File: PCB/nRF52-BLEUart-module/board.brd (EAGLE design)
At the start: 39 x 18 mm, 44 parts, among them J1 USB-A_PTH_MALE, U1 CH340E, U2 NRF52832, Y1 32MHz_2016, Y2 32.768kHz

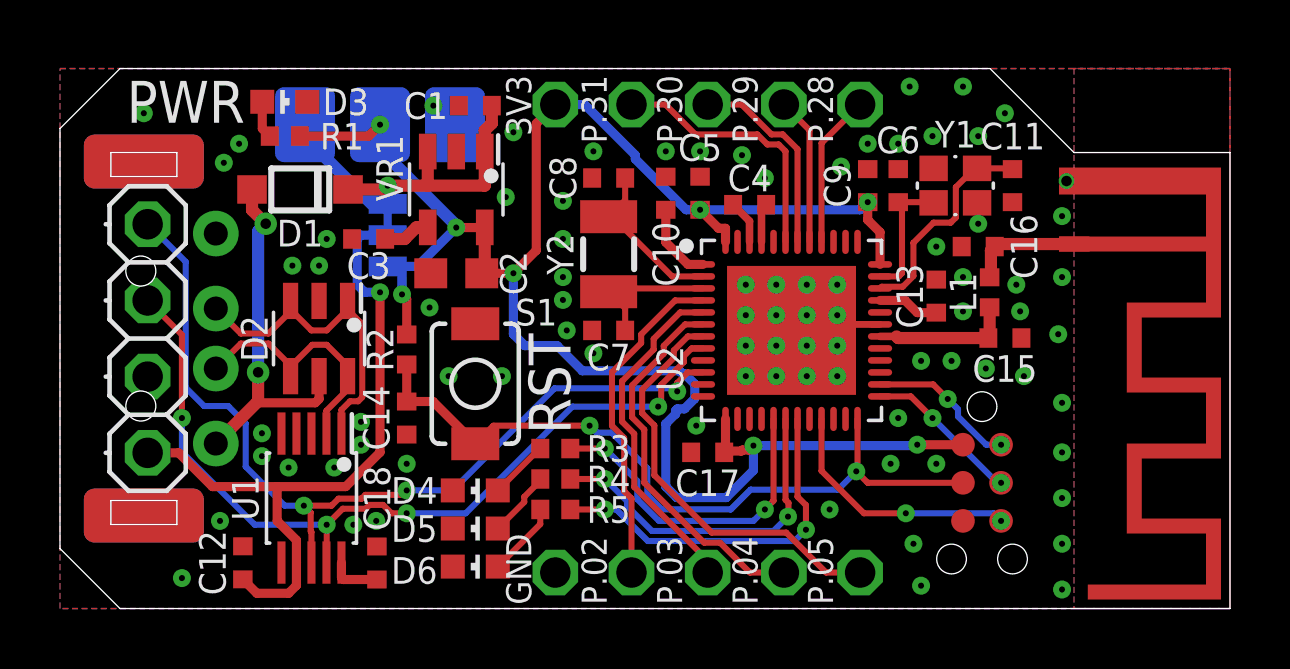
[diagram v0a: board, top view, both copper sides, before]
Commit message: PCB bug fixes, added production files
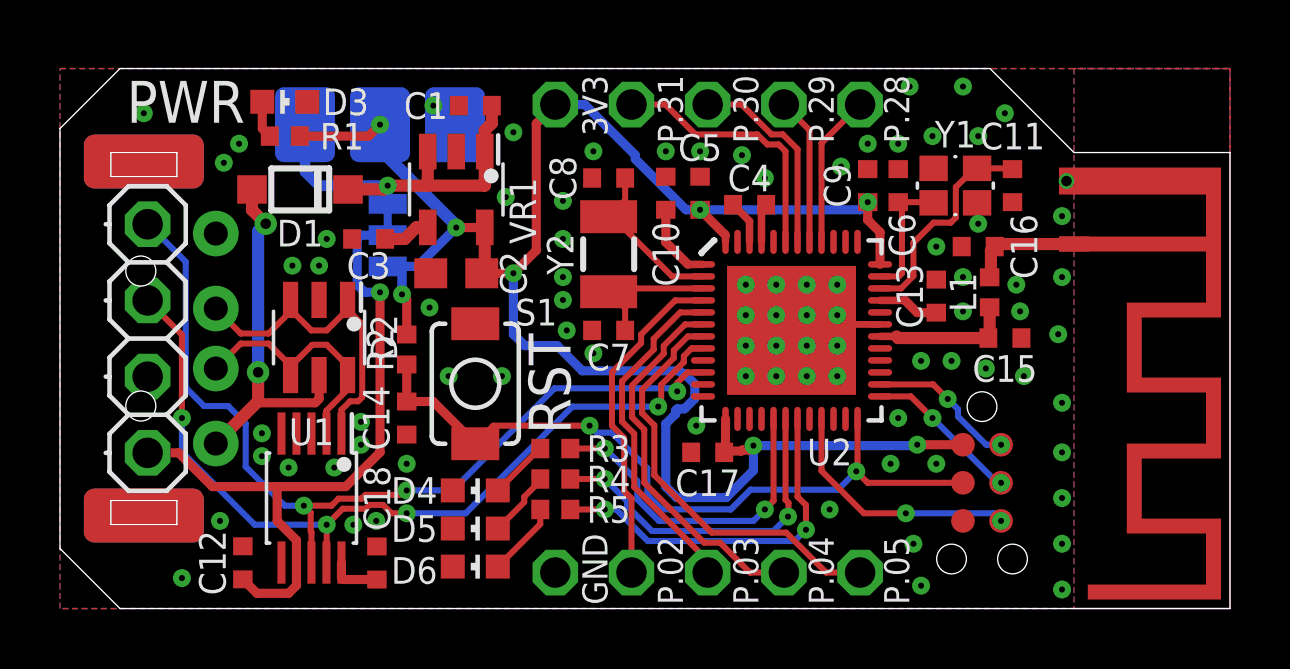
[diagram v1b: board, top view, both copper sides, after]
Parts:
- turned D2 to 270 degrees
- turned U1 to 270 degrees
- turned U2 to 0 degrees
- turned VR1 to 270 degrees
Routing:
- net 5V: track 12.7 -> 13.6 mm
